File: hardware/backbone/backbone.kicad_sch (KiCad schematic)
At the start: 51 parts, among them J1 M20-7810645R, J140 M20-7810645R, J2 FROM_PREVIOUS, J3 M20-7810645R, J9 TO NEXT, Q2 AO3401A, U1 ESP32-S3-WROOM-1_1U_FlexyPin_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, U2 SN65HVD230DR, U3 HC-TYPE-C-16P-01A, U4 AP2112K-3.3TRG1, U5 AP2112K-3.3TRG1, U8 G3VM-61VY3

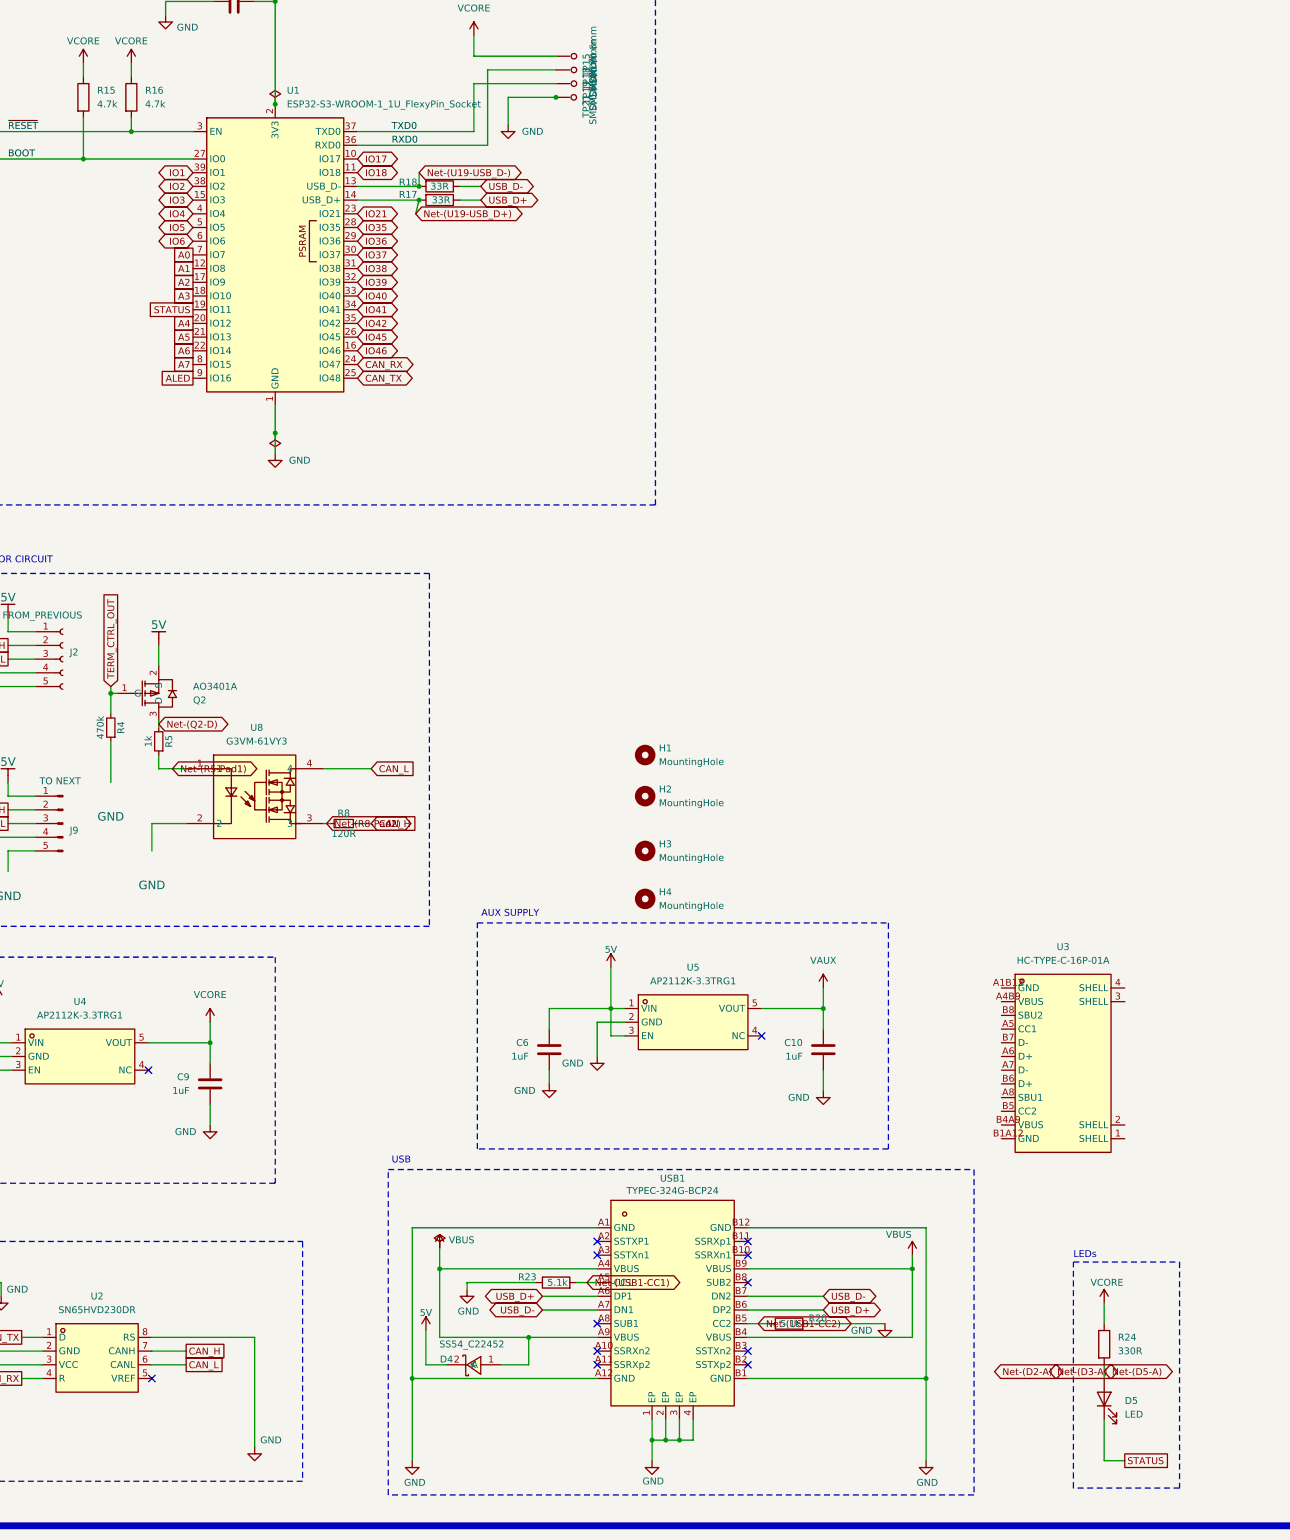
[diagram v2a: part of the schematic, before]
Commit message: Update V3 Backbone schematic and PCB layout
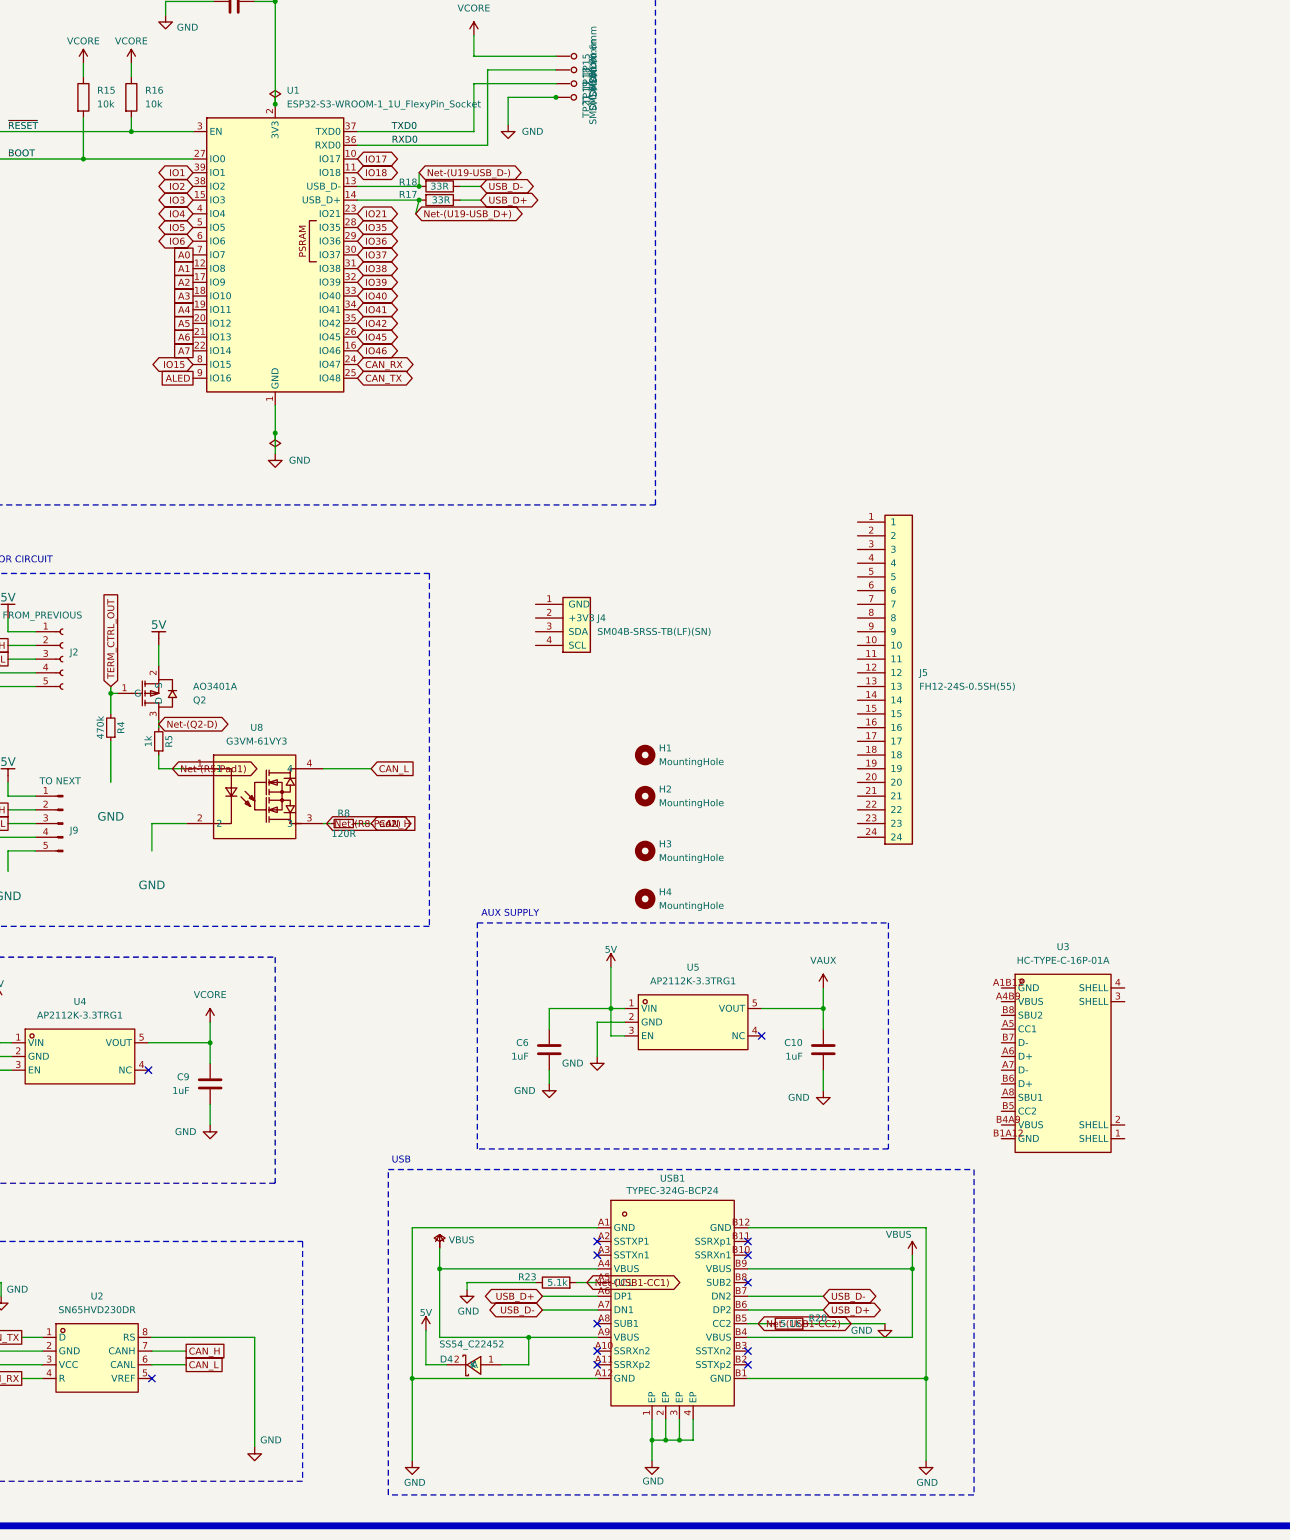
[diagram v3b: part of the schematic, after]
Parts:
- removed D5: LED, SpaghettiLAB:LED0603-RD, symbol Device:LED
- removed R24: 330R, SpaghettiLAB:R0603, symbol Device:R
- added J4: SM04B-SRSS-TB(LF)(SN), SpaghettiLAB:JST_SH_SM04B-SRSS-TB_1x04-1MP_P1.00mm_Horizontal, symbol SpaghettiLAB:Qwiic_JST_SH_4
- added J5: FH12-24S-0.5SH(55), SpaghettiLAB:Hirose_FH12-24S-0.5SH_1x24-1MP_P0.50mm_Horizontal, symbol SpaghettiLAB:FPC_24_Hirose_FH12
- R15, R16: value 4.7k -> 10k
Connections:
- net STATUS is gone; now on net A4: U1.19 (IO11)
- net A4: no longer U1.20 (IO12)
- net A5: now also U1.20 (IO12); no longer U1.21 (IO13)
- net A6: now also U1.21 (IO13); no longer U1.22 (IO14)
- net A7: now also U1.22 (IO14); no longer U1.8 (IO15)
- new net IO15: U1.8 (IO15)
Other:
- note removed: "LEDs"

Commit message: Add camera supplies, DVP connector wiring and Qwiic bus to V3 schematic
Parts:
- added C75, C76, C77, C78: 4.7uF/10V X7R, SpaghettiLAB:C0603, symbol Device:C
- added C79, C80, C81, C82, C83: 100nF, SpaghettiLAB:C0603, symbol Device:C
- added Q3, Q4: BSS138, Package_TO_SOT_SMD:SOT-23, symbol SpaghettiLAB:BSS138
- added R24, R25, R26, R27: 4.7k, SpaghettiLAB:R0603, symbol Device:R
- added R28, R29: 10k, SpaghettiLAB:R0603, symbol Device:R
- added R30: 33R, SpaghettiLAB:R0603, symbol Device:R
- added U10: ME6211C15M5G-N, Package_TO_SOT_SMD:SOT-23-5, symbol SpaghettiLAB:ME6211C15M5G-N
- added U11: SN74LVC1G125DBVR, Package_TO_SOT_SMD:SOT-23-5, symbol SpaghettiLAB:SN74LVC1G125DBVR
- added U9: ME6211C28M5G-N, Package_TO_SOT_SMD:SOT-23-5, symbol SpaghettiLAB:ME6211C28M5G-N
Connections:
- net GND: now also J4.1 (GND), J5.15, J5.2, C75.2, C76.2, C77.2, C78.2, C79.2, C80.2, C81.2, C82.2, C83.2, R29.2, U10.2 (V_{SS}), U11.1, U11.3 (GND), U9.2 (V_{SS})
- net IO1: now also J5.9
- net IO15: now also U11.2
- net IO17: now also J5.16
- net IO18: now also J5.14
- net IO2: now also J5.17
- net IO21: now also J5.12
- net IO38: now also J5.19
- net IO39: now also J5.21
- net IO4: now also J4.3 (SDA), Q3.3 (D), R24.2
- net IO40: now also J5.22
- net IO41: now also J5.20
- net IO42: now also J5.18
- net IO5: now also J4.4 (SCL), Q4.3 (D), R25.2
- net IO6: now also J5.7
- net VAUX: now also C75.1, C77.1, U10.1 (V_{IN}), U10.3 (CE), U9.1 (V_{IN}), U9.3 (CE)
- net VCORE: now also J4.2 (+3V3), C83.1, R24.1, R25.1
- net CAM_1V5: now reaches J5.10
- net CAM_1V5: now also C78.1, C81.1, U10.5 (V_{OUT})
- net CAM_2V8: now reaches J5.11
- net CAM_2V8: now also J5.4, C76.1, C79.1, C80.1, C82.1, Q3.1 (G), Q4.1 (G), R26.1, R27.1, R28.1, U11.5 (VCC), U9.5 (V_{OUT})
- net CAM_XCLK: now reaches J5.13
- net CAM_XCLK: now also R30.2
- net CAM_SDA: now reaches J5.3
- net CAM_SDA: now also Q3.2 (S), R26.2
- net CAM_SCL: now reaches J5.5
- net CAM_SCL: now also Q4.2 (S), R27.2
- net CAM_RESET_N: now reaches J5.6
- net CAM_RESET_N: now also R28.2
- net CAM_PWDN: now reaches J5.8
- net CAM_PWDN: now also R29.1
- new net CAM_XCLK_DRV: R30.1, U11.4
- no-connect marks 14 -> 19
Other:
- note added: "1.5 V DVDD - module dependent"
- note added: "2.8 V AVDD / DOVDD"
- note added: "AVDD 2.8V"
- note added: "C79 at J5.4; C80 at J5.11; C81 at J5.10; C82 at U11.5."
- note added: "CAMERA POWER: VAUX = 3.3 V (U5). Check total camera + LED current."
- note added: "Camera rail limits / module compatibility: see CAMERA-V3.md"
- note added: "Check exact camera flex pinout / orientation before use."
- note added: "D0 / Y2"
- note added: "D1 / Y3"
- note added: "D2 / Y4"
- note added: "D3 / Y5"
- note added: "D4 / Y6"
- note added: "D5 / Y7"
- note added: "D6 / Y8"
- note added: "D7 / Y9"
- note added: "DOVDD 2.8V"
- note added: "DVDD 1.5V"
- note added: "DVP 24P - ESP32-S3-EYE pinout"
- note added: "GND"
- note added: "HREF"
- note added: "NC"
- note added: "PCLK"
- note added: "PWDN"
- note added: "QWIIC: SDA=GPIO4, SCL=GPIO5; 3.3 V only"
- note added: "RESET_N"
- note added: "SCCB level shift 3.3 V <-> 2.8 V"
- note added: "SCL"
- note added: "SDA"
- note added: "VSYNC"
- note added: "XCLK"
- note added: "XCLK GPIO15 -> 2.8 V buffer; RESET high, PWDN low."
- moved on the sheet: J4, J5

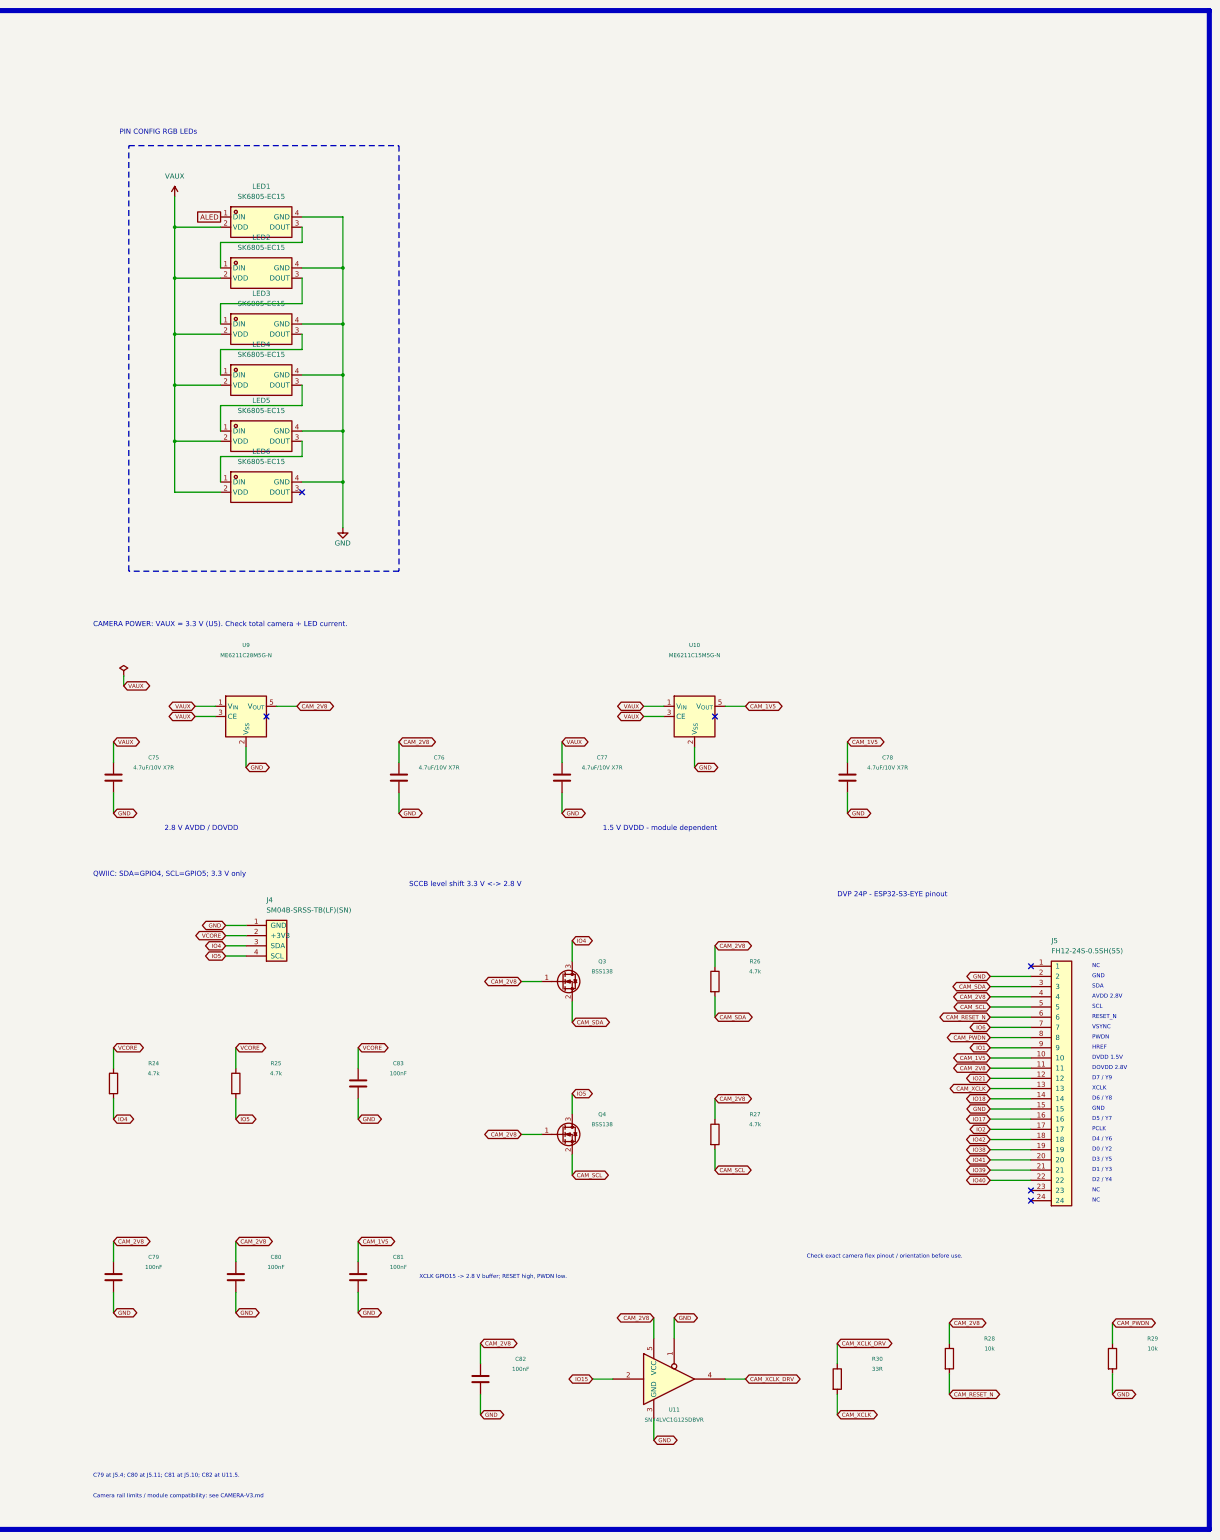
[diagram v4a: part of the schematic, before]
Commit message: Organize camera and Qwiic schematic into commented wired blocks
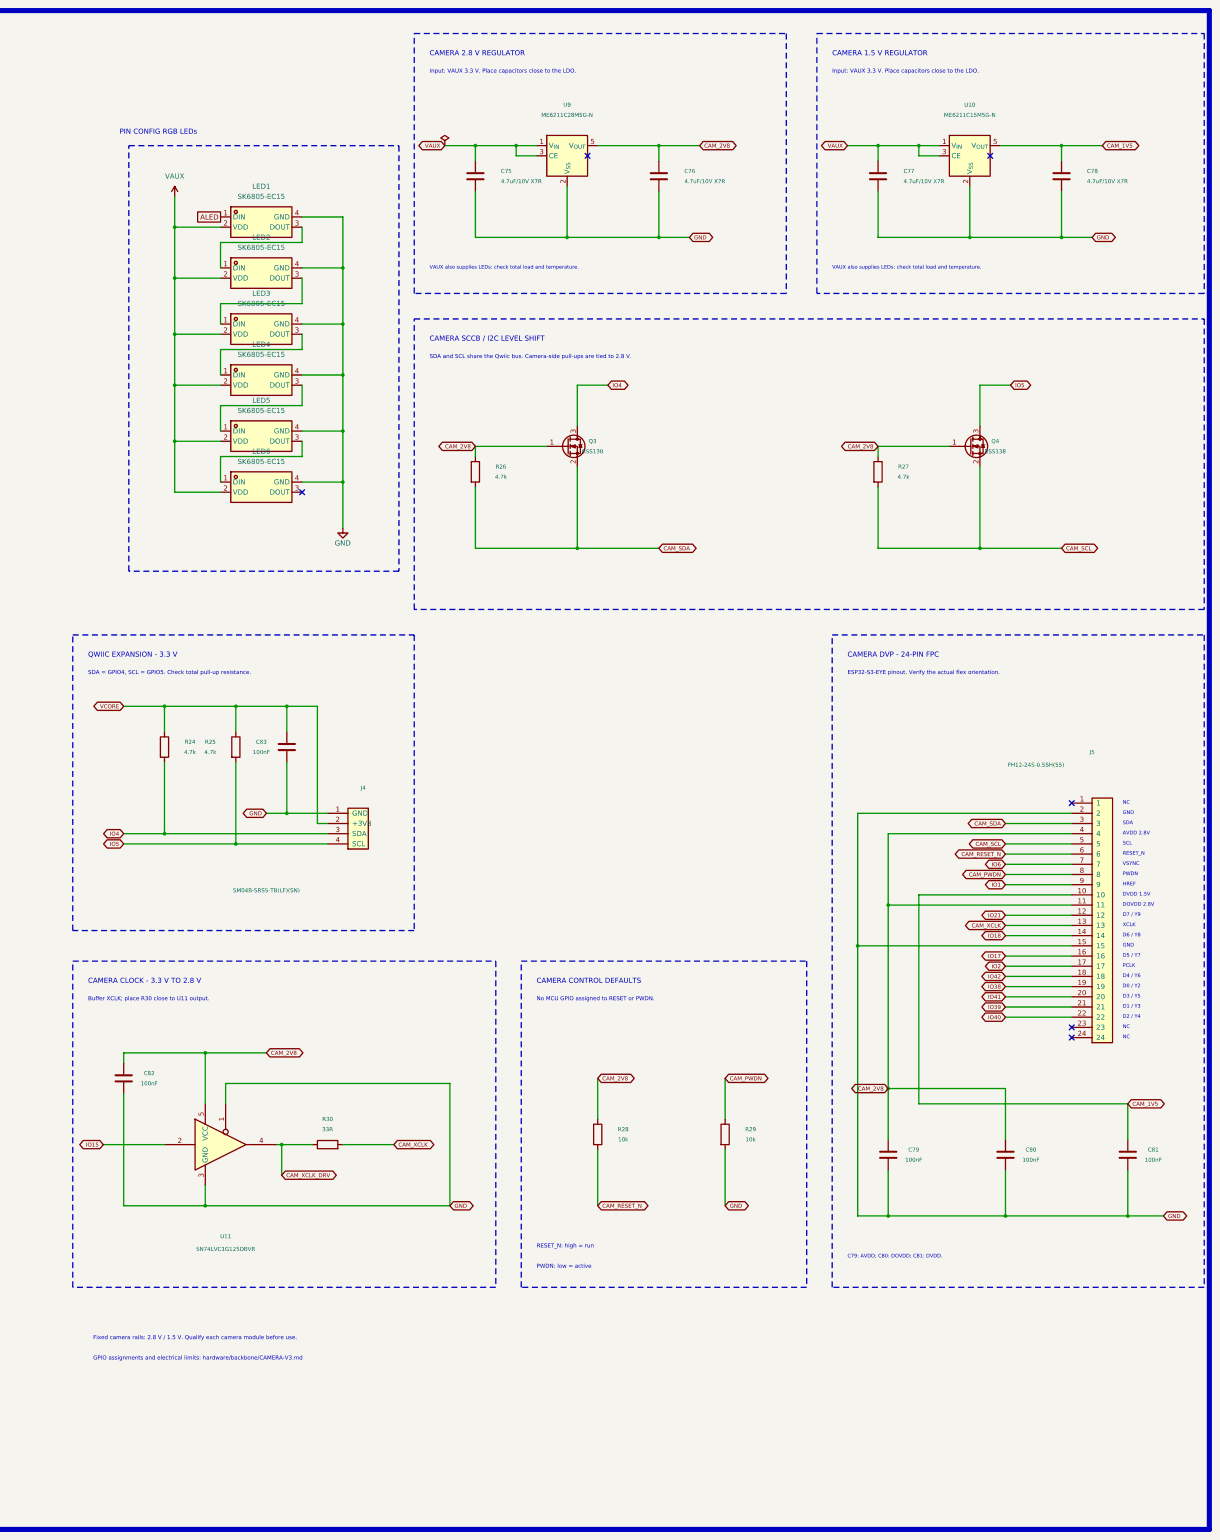
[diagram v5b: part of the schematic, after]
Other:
- note added: "Buffer XCLK; place R30 close to U11 output."
- note added: "C79: AVDD; C80: DOVDD; C81: DVDD."
- note added: "CAMERA 1.5 V REGULATOR"
- note added: "CAMERA 2.8 V REGULATOR"
- note added: "CAMERA CLOCK - 3.3 V TO 2.8 V"
- note added: "CAMERA CONTROL DEFAULTS"
- note added: "CAMERA DVP - 24-PIN FPC"
- note added: "CAMERA SCCB / I2C LEVEL SHIFT"
- note added: "ESP32-S3-EYE pinout. Verify the actual flex orientation."
- note added: "Fixed camera rails: 2.8 V / 1.5 V. Qualify each camera module before use."
- note added: "GPIO assignments and electrical limits: hardware/backbone/CAMERA-V3.md"
- note added: "Input: VAUX 3.3 V. Place capacitors close to the LDO."
- note added: "No MCU GPIO assigned to RESET or PWDN."
- note added: "PWDN: low = active"
- note added: "QWIIC EXPANSION - 3.3 V"
- note added: "RESET_N: high = run"
- note added: "SDA = GPIO4, SCL = GPIO5. Check total pull-up resistance."
- note added: "SDA and SCL share the Qwiic bus. Camera-side pull-ups are tied to 2.8 V."
- note added: "VAUX also supplies LEDs: check total load and temperature."
- note removed: "1.5 V DVDD - module dependent"
- note removed: "2.8 V AVDD / DOVDD"
- note removed: "C79 at J5.4; C80 at J5.11; C81 at J5.10; C82 at U11.5."
- note removed: "CAMERA POWER: VAUX = 3.3 V (U5). Check total camera + LED current."
- note removed: "Camera rail limits / module compatibility: see CAMERA-V3.md"
- note removed: "Check exact camera flex pinout / orientation before use."
- note removed: "DVP 24P - ESP32-S3-EYE pinout"
- note removed: "QWIIC: SDA=GPIO4, SCL=GPIO5; 3.3 V only"
- note removed: "SCCB level shift 3.3 V <-> 2.8 V"
- note removed: "XCLK GPIO15 -> 2.8 V buffer; RESET high, PWDN low."
- moved on the sheet: C75, C76, C77, C78, C79, C80, C81, C82, C83, J4, J5, Q3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

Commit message: Connect camera SCCB directly to Qwiic bus and remove level shifters
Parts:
- removed Q3, Q4: BSS138, Package_TO_SOT_SMD:SOT-23, symbol SpaghettiLAB:BSS138
- removed R26, R27: 4.7k, SpaghettiLAB:R0603, symbol Device:R
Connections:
- net CAM_SCL is gone; now on net IO5: J5.5
- net CAM_SDA is gone; now on net IO4: J5.3
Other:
- note added: "Camera SCCB shares GPIO4/5 directly; pull-ups to 3.3 V."
- note removed: "CAMERA SCCB / I2C LEVEL SHIFT"
- note removed: "SDA = GPIO4, SCL = GPIO5. Check total pull-up resistance."
- note removed: "SDA and SCL share the Qwiic bus. Camera-side pull-ups are tied to 2.8 V."
